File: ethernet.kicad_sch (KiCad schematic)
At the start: 52 parts, among them J301 JK0654219, Q301 BSS138, Q302 BSS138, Q303 BSS138, Q304 BSS138, U301 MIC33050-4YHL, U302 KSZ9031RNXCA, X301 ASE-25.000MHz

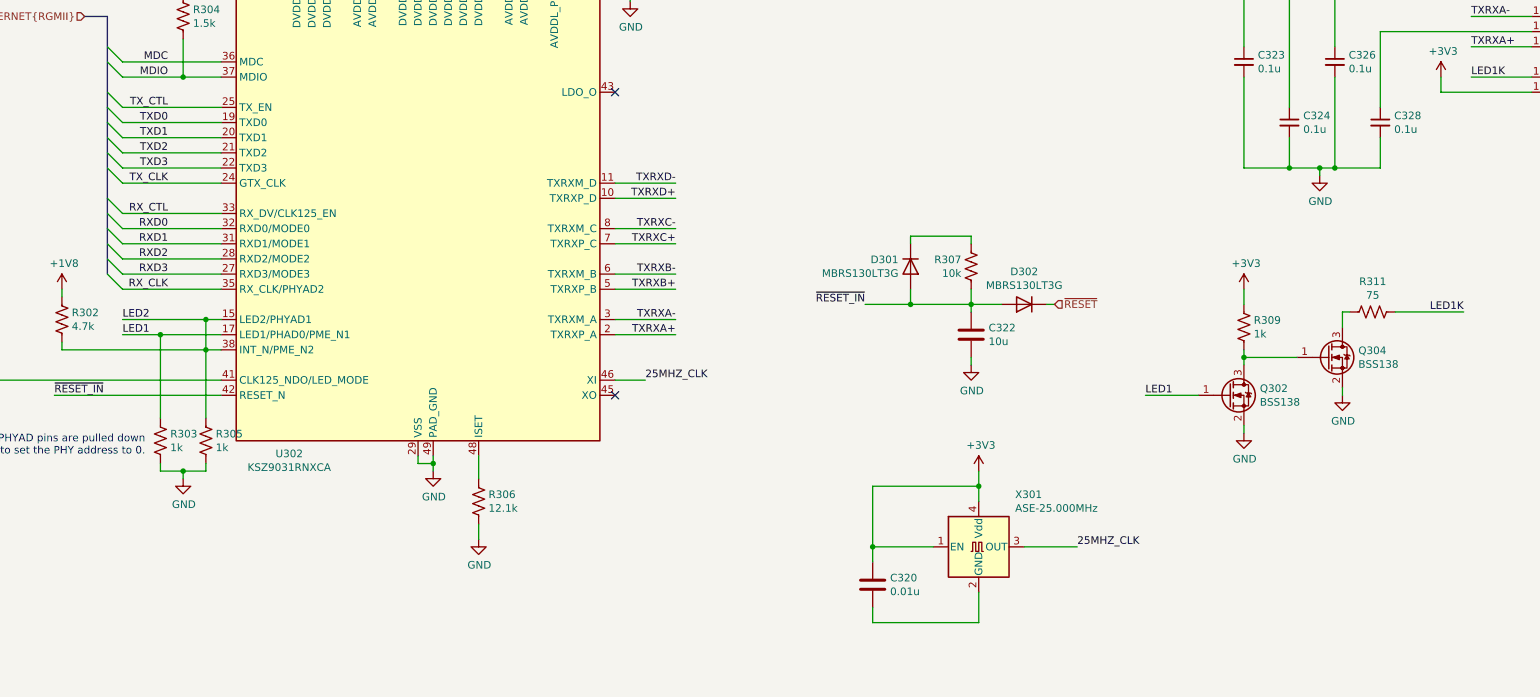
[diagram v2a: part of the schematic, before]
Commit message: Add ULPI USB PHY
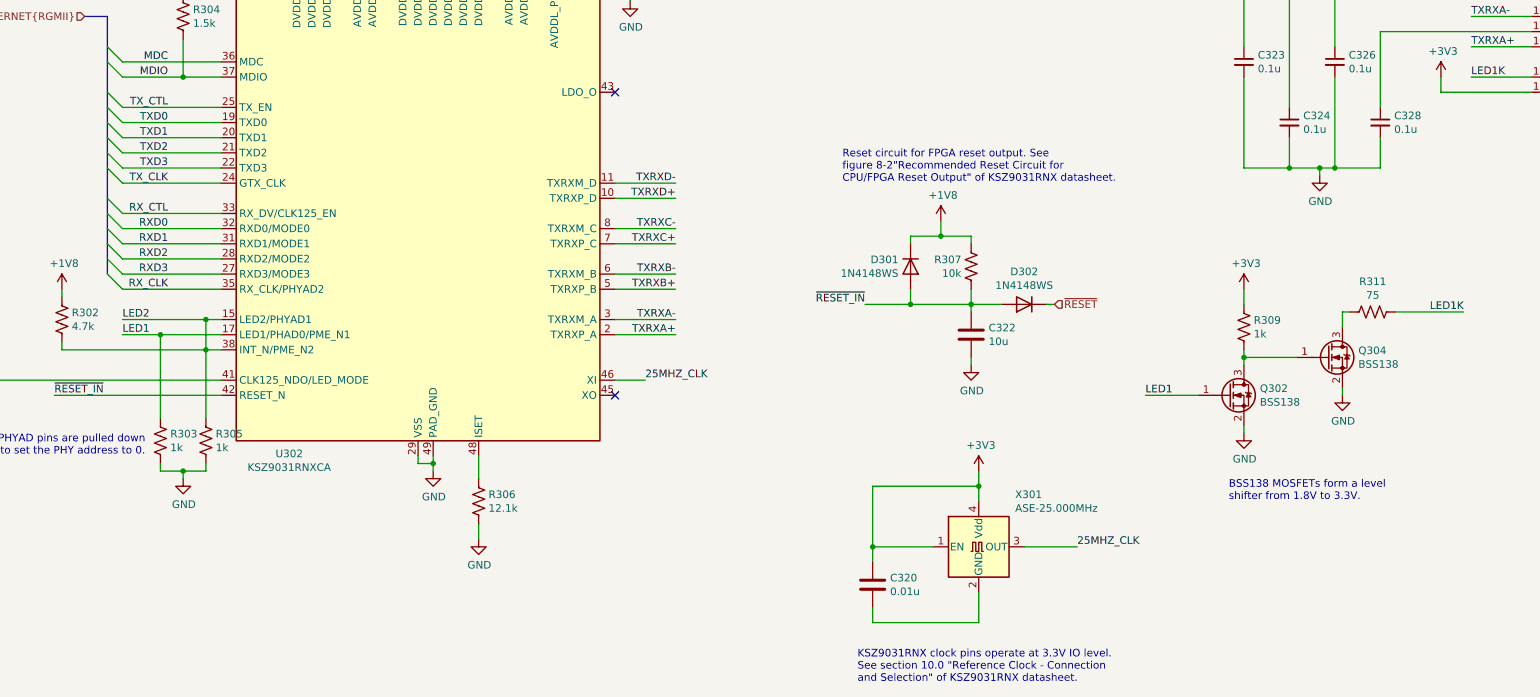
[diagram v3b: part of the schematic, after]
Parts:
- removed D301, D302: MBRS130LT3G, Diode_SMD:D_SMB, symbol Device:D
- added D301, D302: 1N4148WS, Diode_SMD:D_SOD-323, symbol Diode:1N4148WS
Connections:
- net +1V8: now also R307.1, D301.1 (K)
- net ~RESET: now also D302.1 (K)
- net ~RESET_IN: now also D301.2 (A), D302.2 (A)
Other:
- note added: "BSS138 MOSFETs form a level shifter from 1.8V to 3.3V."
- note added: "KSZ9031RNX clock pins operate at 3.3V IO level. See section 10.0 "Reference Clock - Connection and Selection" of KSZ9031RNX datasheet."
- note added: "Reset circuit for FPGA reset output. See figure 8-2"Recommended Reset Circuit for CPU/FPGA Reset Output" of KSZ9031RNX datasheet."
- title: (none) -> Gigabit Ethernet PHY
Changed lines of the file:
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@@
 (kicad_sch (version 20200618) (host eeschema "5.99.0-unknown-77313e4~101~ubuntu20.04.1")
-  (page 3 13)
+  (page 3 14)
   (paper "B")
   (title_block
+    (title "Gigabit Ethernet PHY")
     (date "2020-07-08")
     (rev "1.0")
@@
   (junction (at 232.41 210.82) (diameter 0) (color 0 0 0 0))
   (junction (at 238.76 170.18) (diameter 0) (color 0 0 0 0))
+  (junction (at 243.84 158.75) (diameter 0) (color 0 0 0 0))
   (junction (at 248.92 170.18) (diameter 0) (color 0 0 0 0))
   (junction (at 250.19 200.66) (diameter 0) (color 0 0 0 0))
@@
     (stroke (width 0) (type solid) (color 0 0 0 0))
   )
-  (wire (pts (xy 238.76 158.75) (xy 248.92 158.75))
+  (wire (pts (xy 238.76 158.75) (xy 243.84 158.75))
     (stroke (width 0) (type solid) (color 0 0 0 0))
   )
@@
     (stroke (width 0) (type solid) (color 0 0 0 0))
   )
+  (wire (pts (xy 243.84 156.21) (xy 243.84 158.75))
+    (stroke (width 0) (type solid) (color 0 0 0 0))
+  )
+  (wire (pts (xy 243.84 158.75) (xy 248.92 158.75))
+    (stroke (width 0) (type solid) (color 0 0 0 0))
+  )
   (wire (pts (xy 248.92 158.75) (xy 248.92 160.02))
     (stroke (width 0) (type solid) (color 0 0 0 0))
@@
     (stroke (width 0) (type solid) (color 0 0 0 0))
   )
-  (bus (pts (xy 104.14 137.16) (xy 104.14 139.7))
-    (stroke (width 0) (type solid) (color 0 0 0 0))
-  )
-  (bus (pts (xy 104.14 139.7) (xy 104.14 144.78))
+  (bus (pts (xy 104.14 137.16) (xy 104.14 142.24))
+    (stroke (width 0) (type solid) (color 0 0 0 0))
+  )
+  (bus (pts (xy 104.14 142.24) (xy 104.14 144.78))
     (stroke (width 0) (type solid) (color 0 0 0 0))
   )
@@
     (stroke (width 0) (type solid) (color 0 0 0 0))
   )
-  (bus (pts (xy 104.14 157.48) (xy 104.14 162.56))
-    (stroke (width 0) (type solid) (color 0 0 0 0))
-  )
-  (bus (pts (xy 104.14 162.56) (xy 104.14 165.1))
+  (bus (pts (xy 104.14 157.48) (xy 104.14 160.02))
+    (stroke (width 0) (type solid) (color 0 0 0 0))
+  )
+  (bus (pts (xy 104.14 160.02) (xy 104.14 165.1))
     (stroke (width 0) (type solid) (color 0 0 0 0))
   )
@@
     (effects (font (size 1.27 1.27)) (justify left bottom))
   )
+  (text "Reset circuit for FPGA reset output. See \nfigure 8-2\"Recommended Reset Circuit for\nCPU/FPGA Reset Output\" of KSZ9031RNX datasheet."
+    (at 227.33 149.86 0)
+    (effects (font (size 1.27 1.27)) (justify left bottom))
+  )
+  (text "KSZ9031RNX clock pins operate at 3.3V IO level.\nSee section 10.0 \"Reference Clock - Connection\nand Selection\" of KSZ9031RNX datasheet."
+    (at 229.87 233.68 0)
+    (effects (font (size 1.27 1.27)) (justify left bottom))
+  )
+  (text "BSS138 MOSFETs form a level\nshifter from 1.8V to 3.3V."
+    (at 292.1 203.2 0)
+    (effects (font (size 1.27 1.27)) (justify left bottom))
+  )
   (label "DVDDL" (at 91.44 30.48 180)
     (effects (font (size 1.27 1.27)) (justify right bottom))
@@
     )
     (property "Datasheet" "" (id 3) (at 116.84 116.84 0)
+      (effects (font (size 1.27 1.27)) hide)
+    )
+  )
+  (symbol (lib_id "power:+1V8") (at 243.84 156.21 0) (unit 1)
+    (in_bom yes) (on_board yes)
+    (property "Reference" "#PWR0332" (id 0) (at 243.84 160.02 0)
+      (effects (font (size 1.27 1.27)) hide)
+    )
+    (property "Value" "+1V8" (id 1) (at 244.2083 151.8856 0))
+    (property "Footprint" "" (id 2) (at 243.84 156.21 0)
+      (effects (font (size 1.27 1.27)) hide)
+    )
+    (property "Datasheet" "" (id 3) (at 243.84 156.21 0)
       (effects (font (size 1.27 1.27)) hide)
     )
@@
     )
   )
-  (symbol (lib_id "Device:D") (at 238.76 163.83 270) (unit 1)
+  (symbol (lib_id "Diode:1N4148WS") (at 238.76 163.83 270) (unit 1)
     (in_bom yes) (on_board yes)
     (property "Reference" "D301" (id 0) (at 236.7279 162.6806 90)
       (effects (font (size 1.27 1.27)) (justify right))
     )
-    (property "Value" "MBRS130LT3G" (id 1) (at 236.7279 164.9793 90)
+    (property "Value" "1N4148WS" (id 1) (at 236.7279 164.9793 90)
       (effects (font (size 1.27 1.27)) (justify right))
     )
-    (property "Footprint" "Diode_SMD:D_SMB" (id 2) (at 238.76 163.83 0)
-      (effects (font (size 1.27 1.27)) hide)
-    )
-    (property "Datasheet" "~" (id 3) (at 238.76 163.83 0)
-      (effects (font (size 1.27 1.27)) hide)
-    )
-  )
-  (symbol (lib_id "Device:D") (at 257.81 170.18 180) (unit 1)
+    (property "Footprint" "Diode_SMD:D_SOD-323" (id 2) (at 234.315 163.83 0)
+      (effects (font (size 1.27 1.27)) hide)
+    )
+    (property "Datasheet" "https://www.vishay.com/docs/85751/1n4148ws.pdf" (id 3) (at 238.76 163.83 0)
+      (effects (font (size 1.27 1.27)) hide)
+    )
+  )
+  (symbol (lib_id "Diode:1N4148WS") (at 257.81 170.18 180) (unit 1)
     (in_bom yes) (on_board yes)
     (property "Reference" "D302" (id 0) (at 257.81 164.6998 0))
-    (property "Value" "MBRS130LT3G" (id 1) (at 257.81 166.9985 0))
-    (property "Footprint" "Diode_SMD:D_SMB" (id 2) (at 257.81 170.18 0)
-      (effects (font (size 1.27 1.27)) hide)
-    )
-    (property "Datasheet" "~" (id 3) (at 257.81 170.18 0)
-      (effects (font (size 1.27 1.27)) hide)
-    )
+    (property "Value" "1N4148WS" (id 1) (at 257.81 166.9985 0))
+    (property "Footprint" "Diode_SMD:D_SOD-323" (id 2) (at 257.81 165.735 0)
+      (effects (font (size 1.27 1.27)) hide)
+    )
+    (property "Datasheet" "https://www.vishay.com/docs/85751/1n4148ws.pdf" (id 3) (at 257.81 170.18 0)
+      (effects (font (size 1.27 1.27)) hide)
+    )

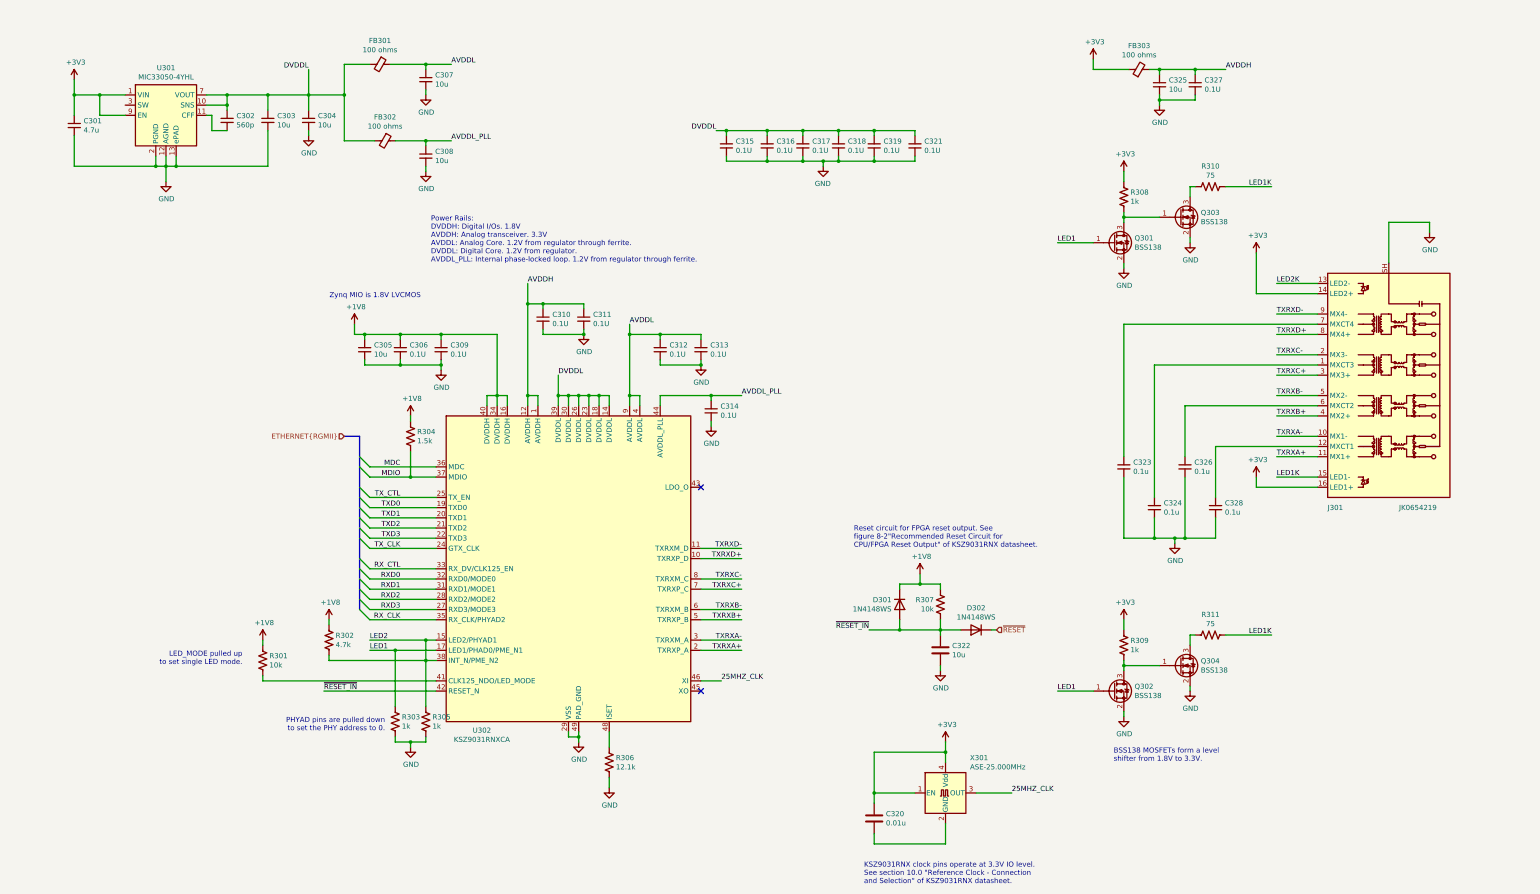
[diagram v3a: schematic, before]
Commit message: Fix footprint associations, use 74LVC2G07 instead of MOSFETs
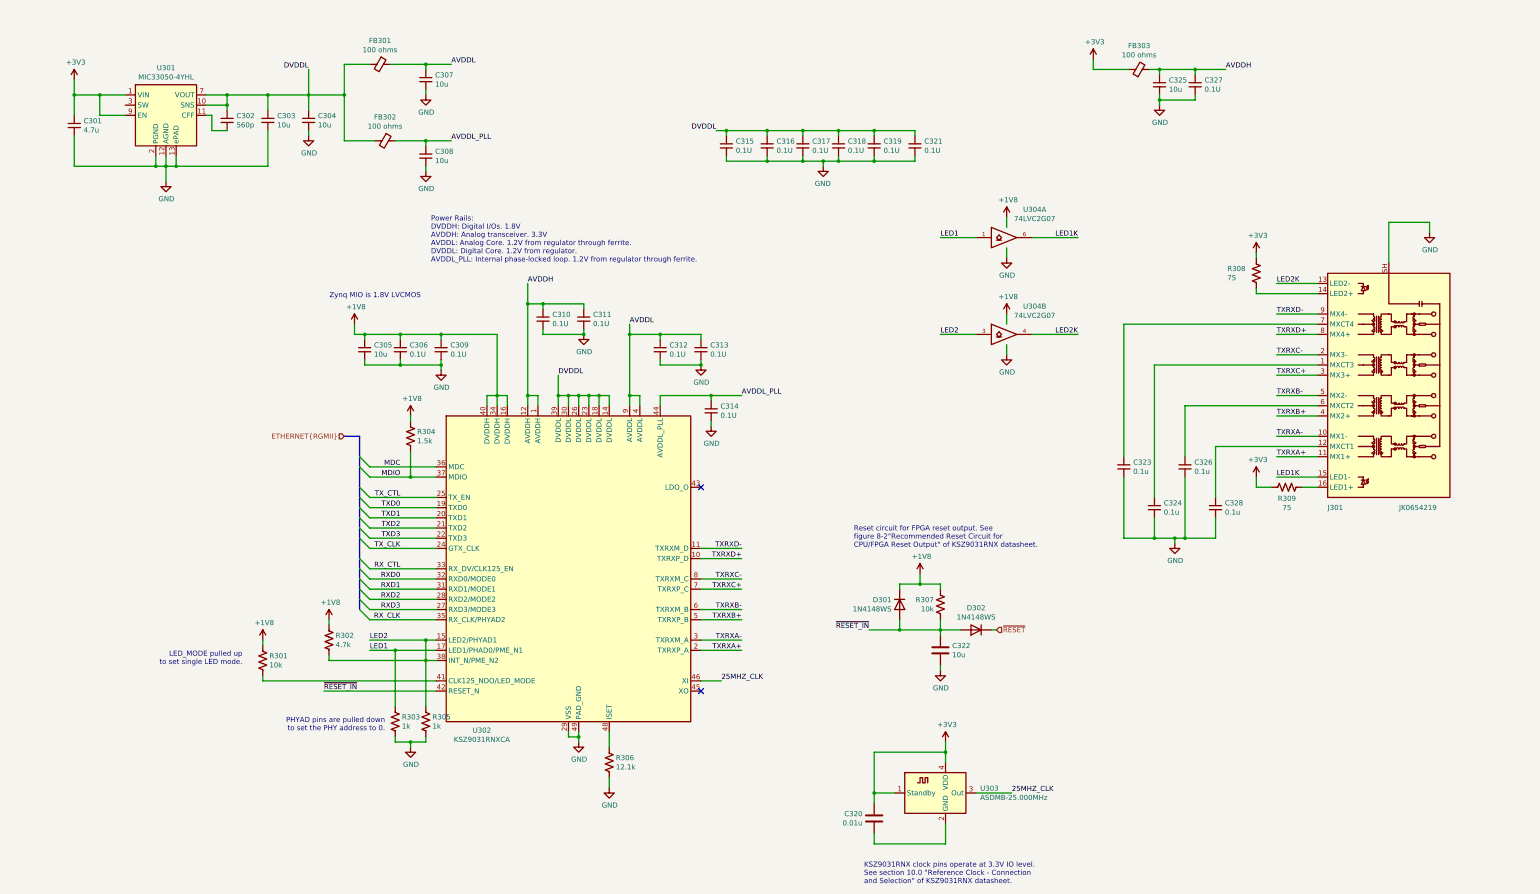
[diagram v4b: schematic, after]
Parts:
- removed Q301, Q302, Q303, Q304: BSS138, Package_TO_SOT_SMD:SOT-23, symbol Transistor_FET:BSS138
- removed R308: 1k, symbol Device:R_US
- removed R311: 75, symbol Device:R_US
- removed X301: ASE-25.000MHz, Oscillator:Oscillator_SMD_Abracon_ASE-4Pin_3.2x2.5mm, symbol Oscillator:ASE-xxxMHz
- added U303: ASDMB-25.000MHz, Oscillator:Oscillator_SMD_Abracon_ASDMB-4Pin_2.5x2.0mm, symbol Oscillator:ASDMB-xxxMHz
- added U304: 74LVC2G07, Package_TO_SOT_SMD:SOT-23-6, symbol 74xGxx:74LVC2G07
- FB301, FB302, FB303: footprint Inductor_SMD:L_6.3x6.3_H3 -> Inductor_SMD:L_0603_1608Metric
- R301, R302, R303, R305: footprint (none) -> Resistor_SMD:R_0402_1005Metric
- R308: renamed from R310; footprint (none) -> Resistor_SMD:R_0402_1005Metric
- R309: value 1k -> 75; footprint (none) -> Resistor_SMD:R_0402_1005Metric
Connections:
- net +1V8: now also U304.5 (VCC), U304.5 (VCC)
- net +3V3: now also R308.2, R309.2, U303.1 (Standby), U303.4 (VDD); no longer J301.14 (LED2+), J301.16 (LED1+), R309.1
- net 25MHZ_CLK: now also U303.3 (Out)
- net GND: now also U304.2 (GND), U304.2 (GND)
- net LED1: now also U304.1
- net LED1K: now also U304.6; no longer R308.2
- net LED2: now also U304.3
- net LED2K: now also U304.4
- net at C320.2: now also U303.2 (GND)
- net at R308.1: now also J301.14 (LED2+)
- new net: J301.16 (LED1+), R309.1
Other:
- note removed: "BSS138 MOSFETs form a level shifter from 1.8V to 3.3V."
- moved on the sheet: R308

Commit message: Connect Ethernet and USB to MIO, start layout
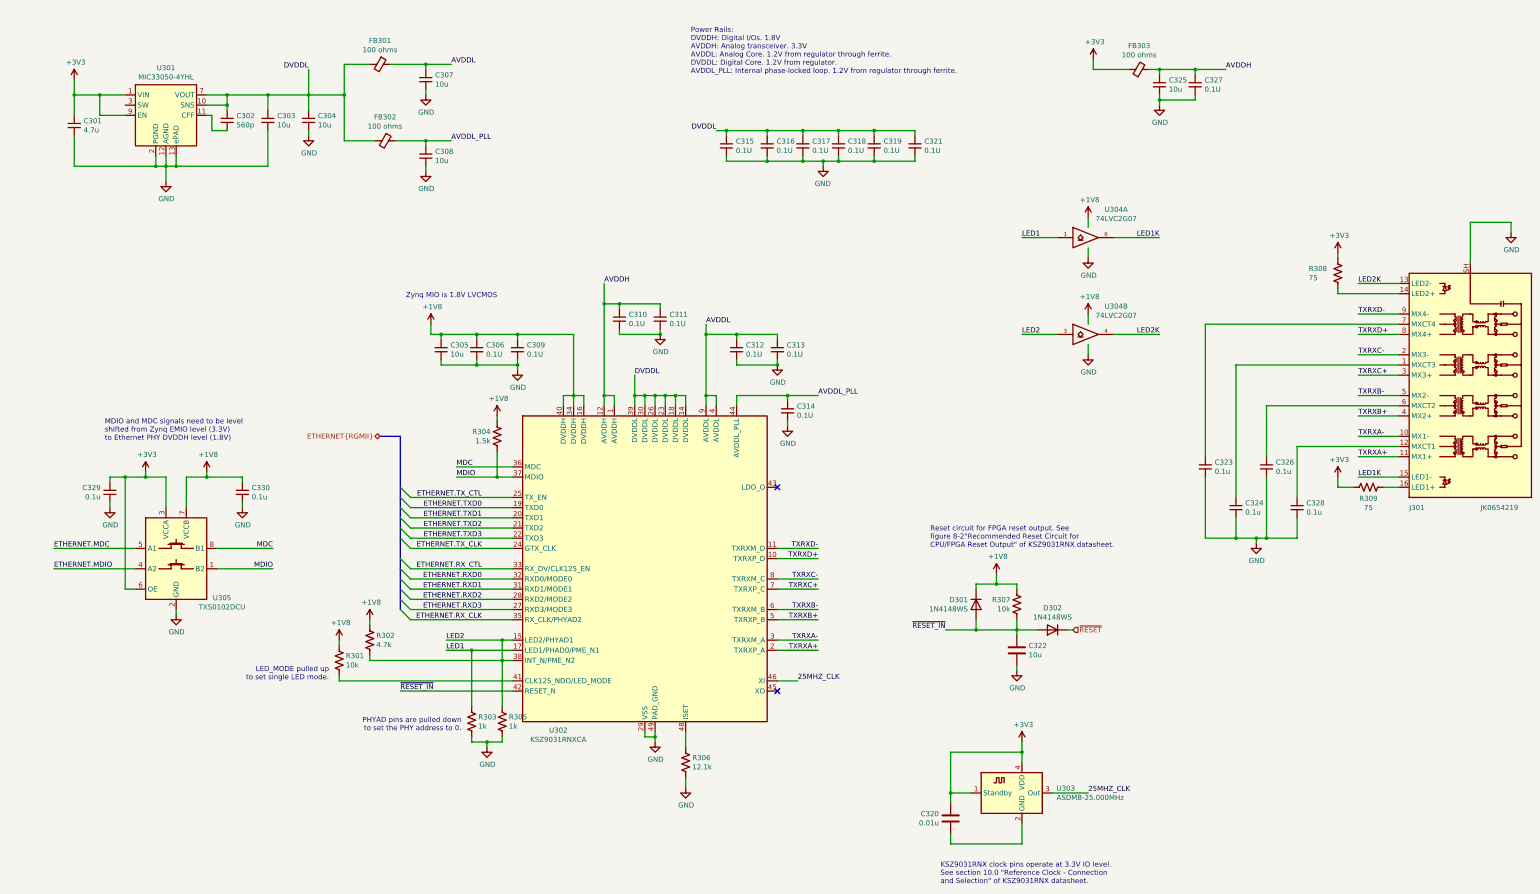
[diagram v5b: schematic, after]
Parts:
- added C329, C330: 0.1u, Capacitor_SMD:C_0603_1608Metric, symbol Device:C_Small
- added U305: TXS0102DCU, Package_SO:VSSOP-8_2.3x2mm_P0.5mm, symbol Logic_LevelTranslator:TXS0102DCU
- C301, C302, C303, C304, C305, C306, C307, C308, C309, C310, C311, C312, C313, C314, C315, C316, C317, C318, C319, C320, C321, C322, C323, C324, C325, C326, C327, C328: footprint Capacitor_SMD:C_0402_1005Metric -> Capacitor_SMD:C_0603_1608Metric
- R301, R302, R303, R304, R305, R306, R307, R308, R309: footprint Resistor_SMD:R_0402_1005Metric -> Resistor_SMD:R_0603_1608Metric
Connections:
- net +1V8: now also C330.1, U305.7 (VCCB)
- net +3V3: now also C329.2, U305.3 (VCCA), U305.6 (OE)
- net GND: now also C329.1, C330.2, U305.2 (GND)
- net MDC: now also U305.8 (B1)
- net MDIO: now also U305.1 (B2)
- net RXD0 renamed ETHERNET.RXD0
- net RXD1 renamed ETHERNET.RXD1
- net RXD2 renamed ETHERNET.RXD2
- net RXD3 renamed ETHERNET.RXD3
- net RX_CLK renamed ETHERNET.RX_CLK
- net RX_CTL renamed ETHERNET.RX_CTL
- net TXD0 renamed ETHERNET.TXD0
- net TXD1 renamed ETHERNET.TXD1
- net TXD2 renamed ETHERNET.TXD2
- net TXD3 renamed ETHERNET.TXD3
- net TX_CLK renamed ETHERNET.TX_CLK
- net TX_CTL renamed ETHERNET.TX_CTL
- new net ETHERNET.MDC: U305.5 (A1)
- new net ETHERNET.MDIO: U305.4 (A2)
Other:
- note added: "MDIO and MDC signals need to be level shifted from Zynq EMIO level (3.3V) to Ethernet PHY DVDDH level (1.8V)"
- moved on the sheet: C305, C306, C309, C310, C311, C312, C313, C314, C320, C322, C323, C324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
